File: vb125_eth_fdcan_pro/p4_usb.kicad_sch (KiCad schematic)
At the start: 29 parts, among them J5 USB_C_Receptacle_USB2.0, U3 NCP563SQ18T1G, U4 USB3315, X1 24MHz

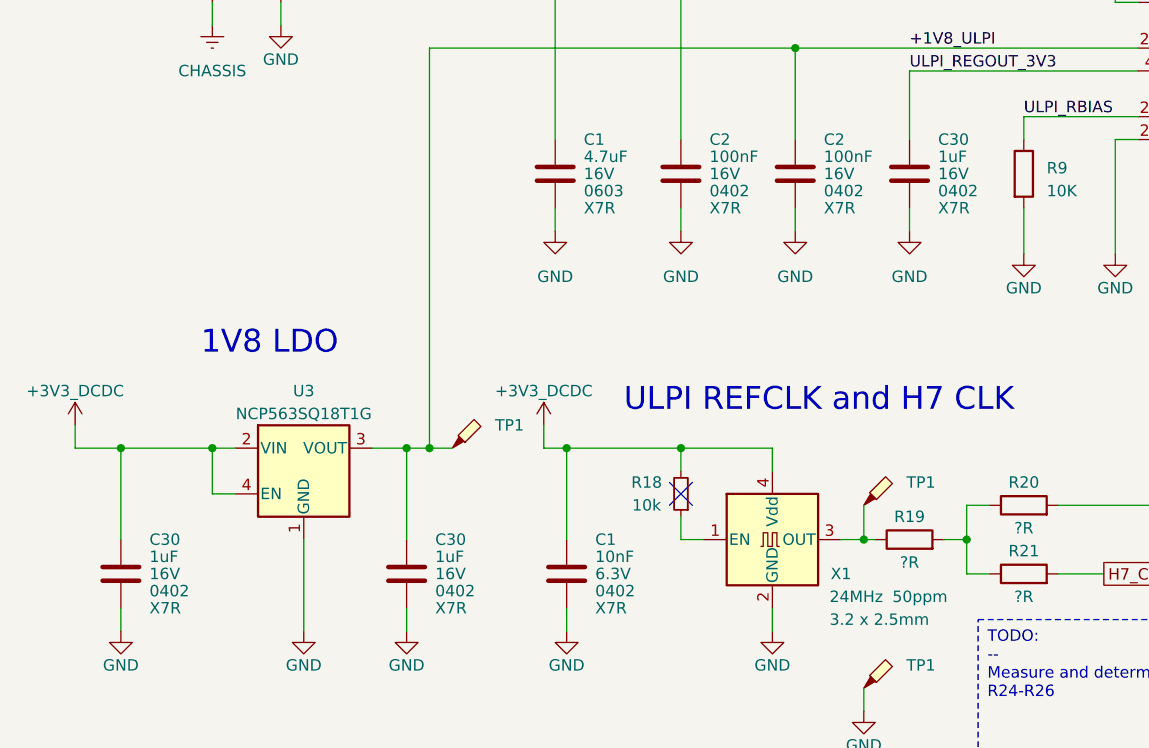
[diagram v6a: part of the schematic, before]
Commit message: Selection of capacitors for VB125
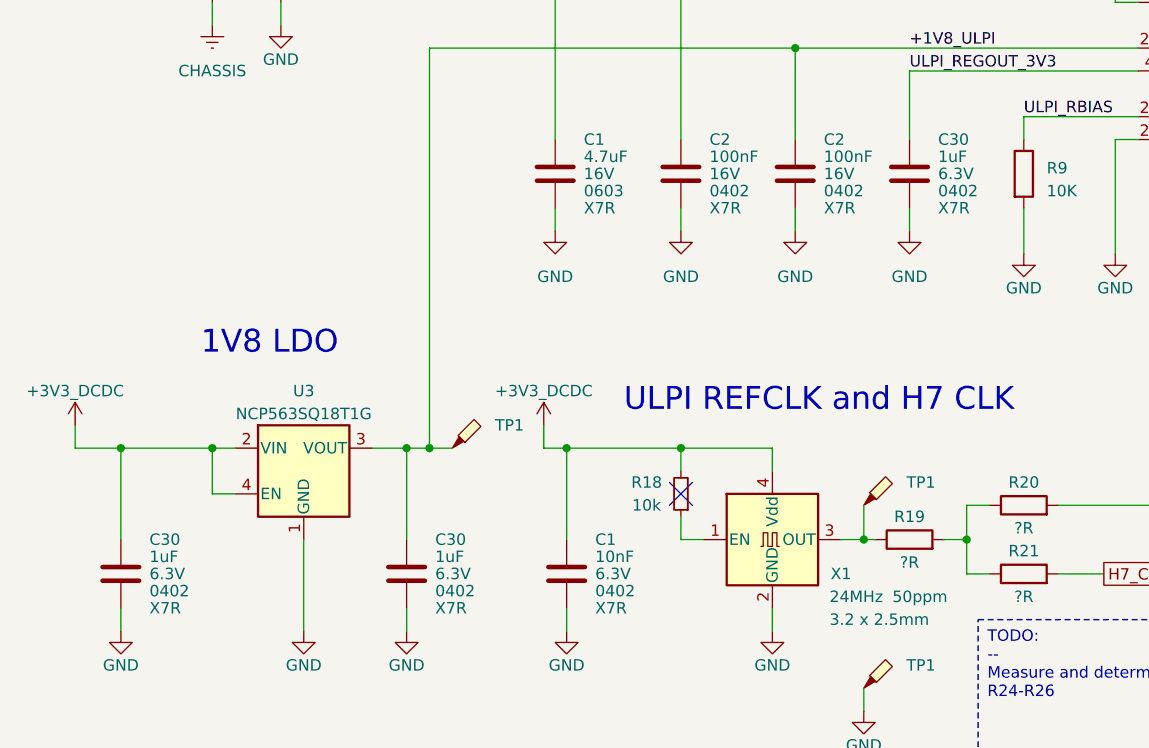
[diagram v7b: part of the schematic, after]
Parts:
- C1: Mpn1 (none) -> CL05B103KB5NNNC; Mpn2 (none) -> CC0402KRX7R9BB103
- C1: Mpn1 (none) -> Murata:GRM188Z71C475KE21J; Mpn2 (none) -> Murata:GRM188Z71C475KE21D
- C1: Mpn1 (none) -> 0402B103K6R3CT; Mpn2 (none) -> 04026C103KAT2A
- C2: Mpn1 (none) -> Samsung:CL05B104KQ5NNNC; Mpn2 (none) -> YAGEO:CC0402KRX7R5BB104
- C30: Mpn1 (none) -> Murata:GRM155R70J105KA12D; Mpn2 (none) -> Murata:GRM155R70J105KA12J; Voltage 16V -> 6.3V
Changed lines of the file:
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@@
+      (effects (font (size 1.27 1.27)) hide)
+    )
+    (property "Mpn1" "CL05B103KB5NNNC" (at 167.64 68.58 0)
+      (effects (font (size 1.27 1.27)) hide)
+    )
+    (property "Mpn2" "CC0402KRX7R9BB103" (at 167.64 68.58 0)
       (effects (font (size 1.27 1.27)) hide)
     )
@@
       (effects (font (size 1.27 1.27)) hide)
     )
+    (property "Mpn1" "CL05B103KB5NNNC" (at 190.5 68.58 0)
+      (effects (font (size 1.27 1.27)) hide)
+    )
+    (property "Mpn2" "CC0402KRX7R9BB103" (at 190.5 68.58 0)
+      (effects (font (size 1.27 1.27)) hide)
+    )
     (pin "1")
     (pin "2")
@@
       (effects (font (size 1.27 1.27)) hide)
     )
-    (property "Voltage" "16V" (at 130.175 194.31 0)
+    (property "Voltage" "6.3V" (at 130.175 194.31 0)
       (effects (font (size 1.27 1.27)) (justify left))
     )
@@
     )
     (property "Vworking" "?" (at 127 194.31 0)
+      (effects (font (size 1.27 1.27)) hide)
+    )
+    (property "Mpn1" "Murata:GRM155R70J105KA12D" (at 127 194.31 0)
+      (effects (font (size 1.27 1.27)) hide)
+    )
+    (property "Mpn2" "Murata:GRM155R70J105KA12J" (at 127 194.31 0)
       (effects (font (size 1.27 1.27)) hide)
     )
@@
     )
     (property "Field8" "" (at 179.07 68.58 0)
+      (effects (font (size 1.27 1.27)) hide)
+    )
+    (property "Mpn1" "CL05B103KB5NNNC" (at 179.07 68.58 0)
+      (effects (font (size 1.27 1.27)) hide)
+    )
+    (property "Mpn2" "CC0402KRX7R9BB103" (at 179.07 68.58 0)
       (effects (font (size 1.27 1.27)) hide)
     )
@@
       (effects (font (size 1.27 1.27)) hide)
     )
-    (property "Voltage" "16V" (at 217.805 149.86 0)
+    (property "Voltage" "6.3V" (at 217.805 149.86 0)
       (effects (font (size 1.27 1.27)) (justify left))
     )
@@
       (effects (font (size 1.27 1.27)) hide)
     )
+    (property "Mpn1" "Murata:GRM155R70J105KA12D" (at 214.63 149.86 0)
+      (effects (font (size 1.27 1.27)) hide)
+    )
+    (property "Mpn2" "Murata:GRM155R70J105KA12J" (at 214.63 149.86 0)
+      (effects (font (size 1.27 1.27)) hide)
+    )
     (pin "1")
     (pin "2")
@@
       (effects (font (size 1.27 1.27)) hide)
     )
+    (property "Mpn1" "Samsung:CL05B104KQ5NNNC  " (at 201.93 149.86 0)
+      (effects (font (size 1.27 1.27)) hide)
+    )
+    (property "Mpn2" "YAGEO:CC0402KRX7R5BB104" (at 201.93 149.86 0)
+      (effects (font (size 1.27 1.27)) hide)
+    )
     (pin "1")
     (pin "2")
@@
     )
     (property "Field8" "" (at 201.93 68.58 0)
+      (effects (font (size 1.27 1.27)) hide)
+    )
+    (property "Mpn1" "CL05B103KB5NNNC" (at 201.93 68.58 0)
+      (effects (font (size 1.27 1.27)) hide)
+    )
+    (property "Mpn2" "CC0402KRX7R9BB103" (at 201.93 68.58 0)
       (effects (font (size 1.27 1.27)) hide)
     )
@@
       (effects (font (size 1.27 1.27)) hide)
     )
-    (property "Voltage" "16V" (at 161.925 194.31 0)
+    (property "Voltage" "6.3V" (at 161.925 194.31 0)
       (effects (font (size 1.27 1.27)) (justify left))
     )
@@
       (effects (font (size 1.27 1.27)) hide)
     )
+    (property "Mpn1" "Murata:GRM155R70J105KA12D" (at 158.75 194.31 0)
+      (effects (font (size 1.27 1.27)) hide)
+    )
+    (property "Mpn2" "Murata:GRM155R70J105KA12J" (at 158.75 194.31 0)
+      (effects (font (size 1.27 1.27)) hide)
+    )
     (pin "1")
     (pin "2")
@@
     )
     (property "Vworking" "3.3V" (at 189.23 149.86 0)
+      (effects (font (size 1.27 1.27)) hide)
+    )
+    (property "Mpn1" "Samsung:CL05B104KQ5NNNC  " (at 189.23 149.86 0)
+      (effects (font (size 1.27 1.27)) hide)
+    )
+    (property "Mpn2" "YAGEO:CC0402KRX7R5BB104" (at 189.23 149.86 0)
       (effects (font (size 1.27 1.27)) hide)
     )
@@
       (effects (font (size 1.27 1.27)) hide)
     )
+    (property "Mpn1" "Murata:GRM188Z71C475KE21J" (at 175.26 149.86 0)
+      (effects (font (size 1.27 1.27)) hide)
+    )
+    (property "Mpn2" "Murata:GRM188Z71C475KE21D" (at 175.26 149.86 0)
+      (effects (font (size 1.27 1.27)) hide)
+    )
     (pin "1")
     (pin "2")
@@
       (effects (font (size 1.27 1.27)) hide)
     )
+    (property "Mpn1" "0402B103K6R3CT" (at 176.53 194.31 0)
+      (effects (font (size 1.27 1.27)) hide)
+    )
+    (property "Mpn2" "04026C103KAT2A" (at 176.53 194.31 0)
+      (effects (font (size 1.27 1.27)) hide)
+    )

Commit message: Finish layout.
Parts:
- added D16: RCLAMP0502BA, Package_TO_SOT_SMD:SOT-416, symbol Power_Protection:RCLAMP0502BA
- added TP1: TestPoint_Probe, TestPoint:TestPoint_Pad_D1.5mm, symbol Connector:TestPoint_Probe
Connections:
- net +VIN_USB: now also TP1.1
- net CHASSIS: now also D16.3 (A)
- net DM renamed D_N
- net D_N: now also D16.1 (K1)
- net DP renamed D_P
- net D_P: now also D16.2 (K2)
- net USBFS_DM renamed USBFS_D_N
- net USBFS_DP renamed USBFS_D_P
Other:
- moved on the sheet: C1, D2, J5, R19
